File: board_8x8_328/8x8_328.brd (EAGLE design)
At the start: 100 x 100 mm, 104 parts, among them IC1 74HC595N, IC2 74HC595N, IC4 74AC164N, Q1 MOSFET-NCHANNEL2N7000, Q10 BS250, Q11 BS250, Q12 BS250, Q13 BS250, Q14 BS250, Q15 BS250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

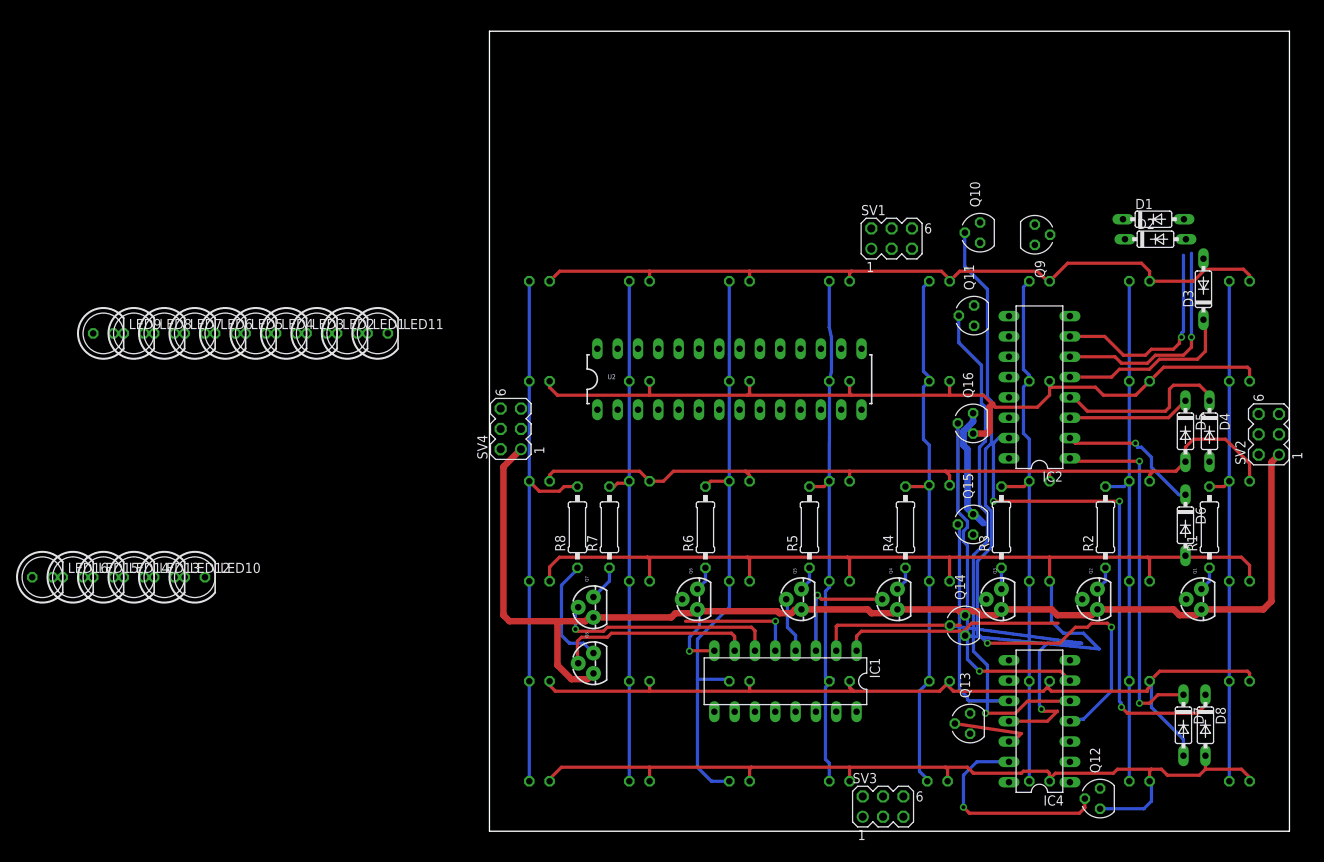
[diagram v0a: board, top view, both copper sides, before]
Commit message: postioning components to the top edge
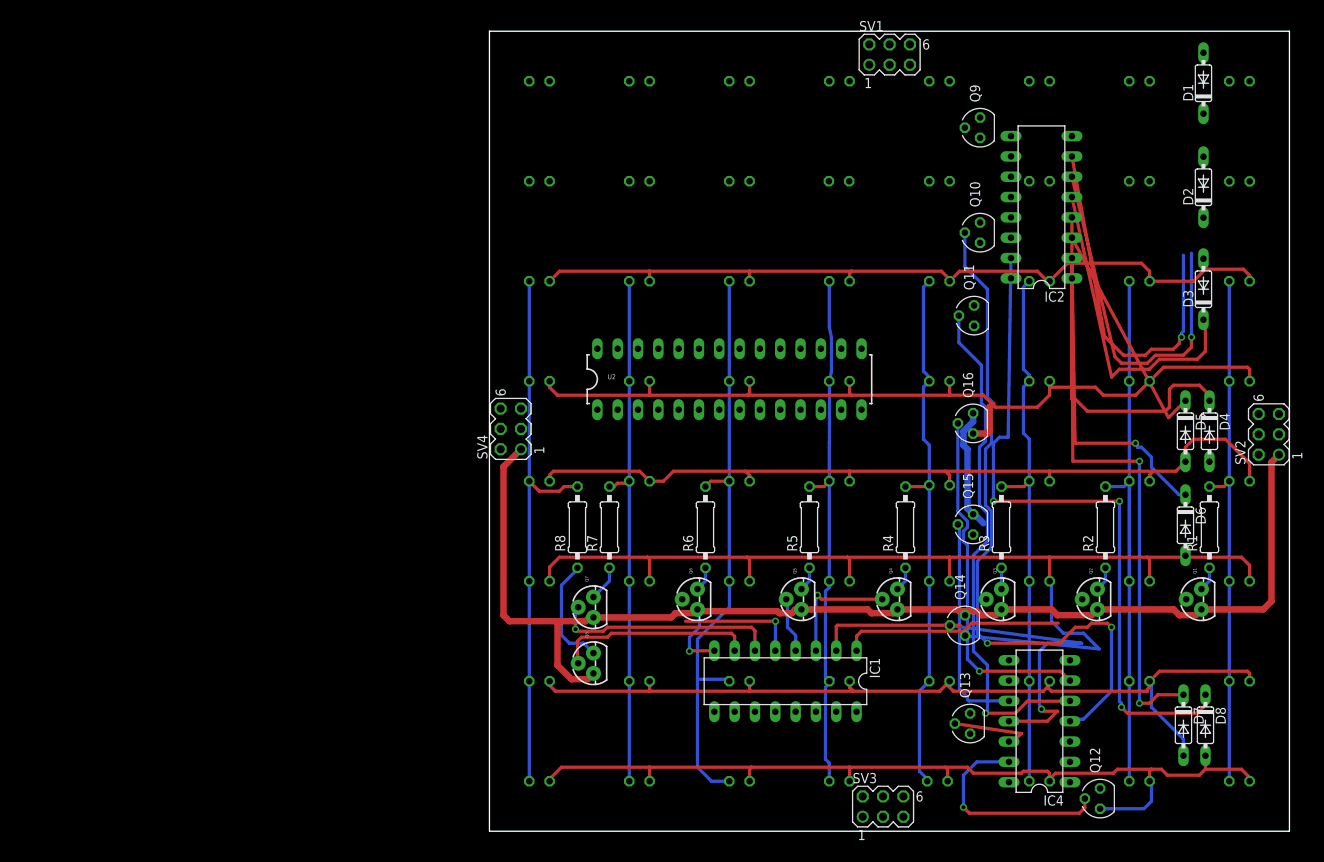
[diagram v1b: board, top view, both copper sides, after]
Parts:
- moved LED9 143.3 mm to (93.8, 81.2), flipped to the bottom
- moved LED10 128.0 mm to (81.2, 81.2), flipped to the bottom
- moved LED1 115.9 mm to (93.8, 93.8), flipped to the bottom
- moved LED12 108.8 mm to (56.2, 81.2), flipped to the bottom
- moved LED2 107.6 mm to (81.2, 93.8), flipped to the bottom
- moved LED13 101.1 mm to (43.7, 81.2), flipped to the bottom
- moved LED3 99.3 mm to (68.8, 93.8), flipped to the bottom
- moved LED14 93.7 mm to (31.2, 81.2), flipped to the bottom
- moved LED4 91.1 mm to (56.2, 93.8), flipped to the bottom
- moved LED15 86.4 mm to (18.8, 81.2), flipped to the bottom
- moved LED11 84.9 mm to (68.8, 81.2), flipped to the bottom
- moved LED5 83.0 mm to (43.8, 93.8), flipped to the bottom
- moved LED16 79.4 mm to (6.25, 81.2), flipped to the bottom
- moved LED6 75.0 mm to (31.2, 93.8), flipped to the bottom
- moved LED7 67.2 mm to (18.8, 93.8), flipped to the bottom
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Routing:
- net N$24: track 22.0 -> 44.4 mm
- net N$21: track 45.0 -> 67.4 mm
- net N$20: track 63.7 -> 85.9 mm
- net N$22: track 18.3 -> 40.5 mm
- net N$14: track 26.5 -> 45.0 mm
- net N$25: track 22.3 -> 40.2 mm
- net N$26: track 28.1 -> 45.6 mm
- net N$23: track 15.3 -> 28.5 mm
